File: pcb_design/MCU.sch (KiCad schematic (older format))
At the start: 14 parts, among them U1 STM32F40X_LQFP64, X2 ABM3B - 8MHz

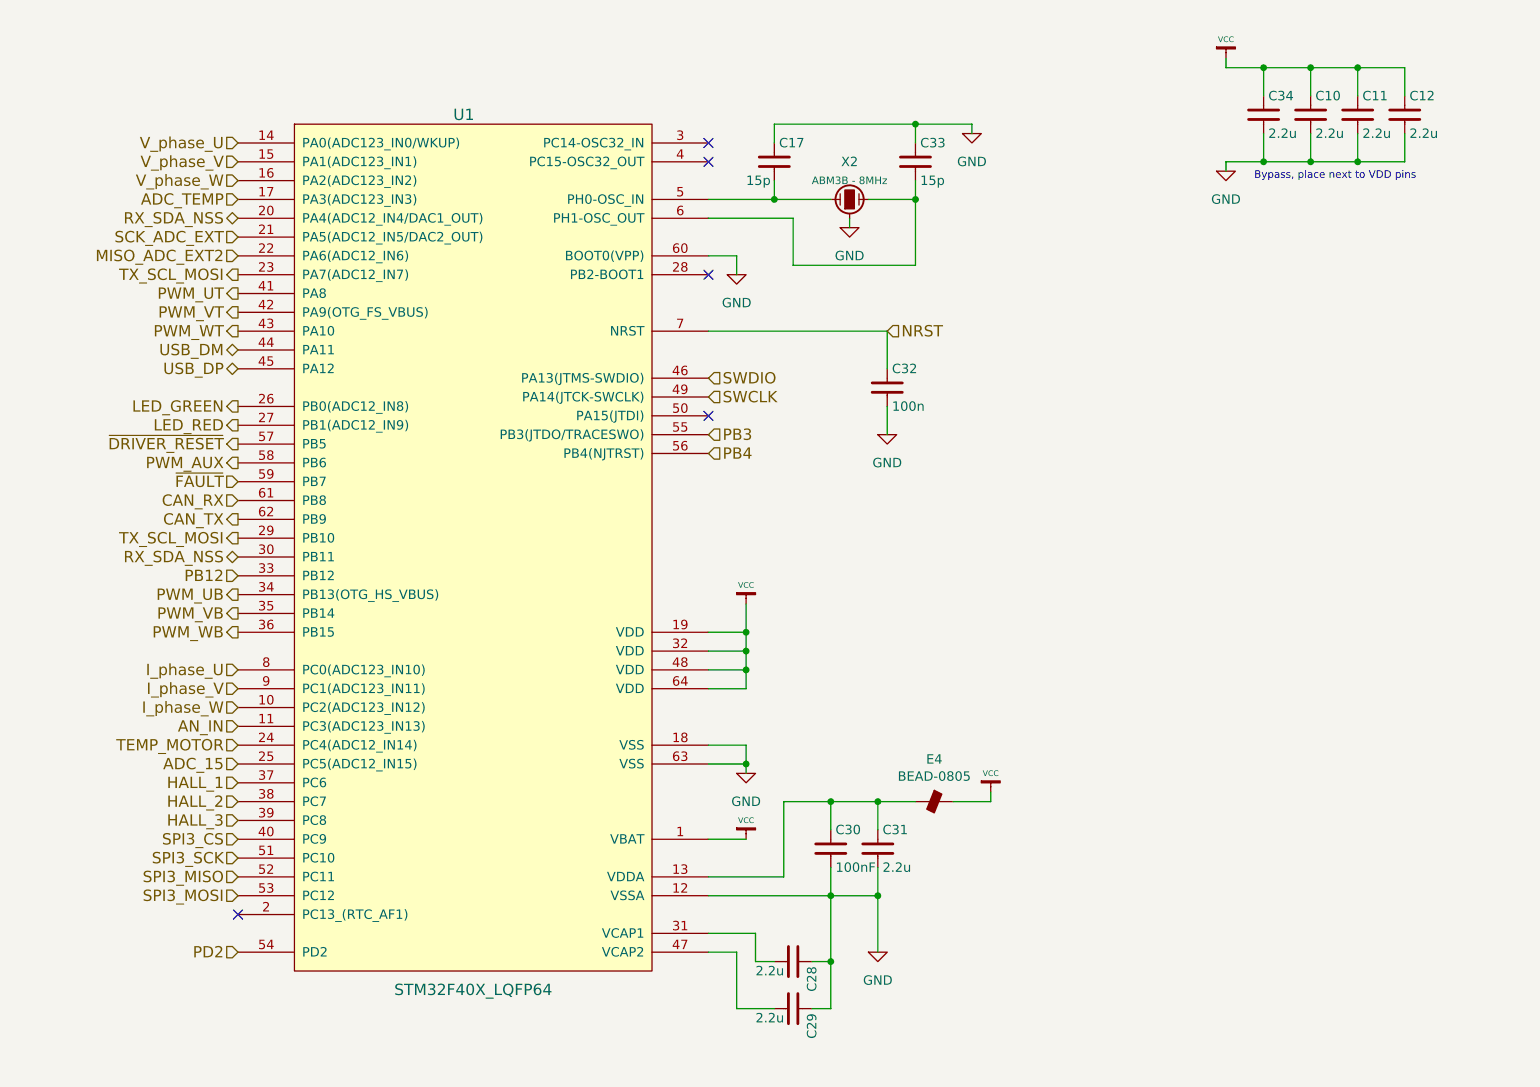
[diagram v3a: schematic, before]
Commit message: Added lp filters, fuses, tvs and power symbols
Signed-off-by: Marcos Chaparro <mchaparro@paltatech.com>
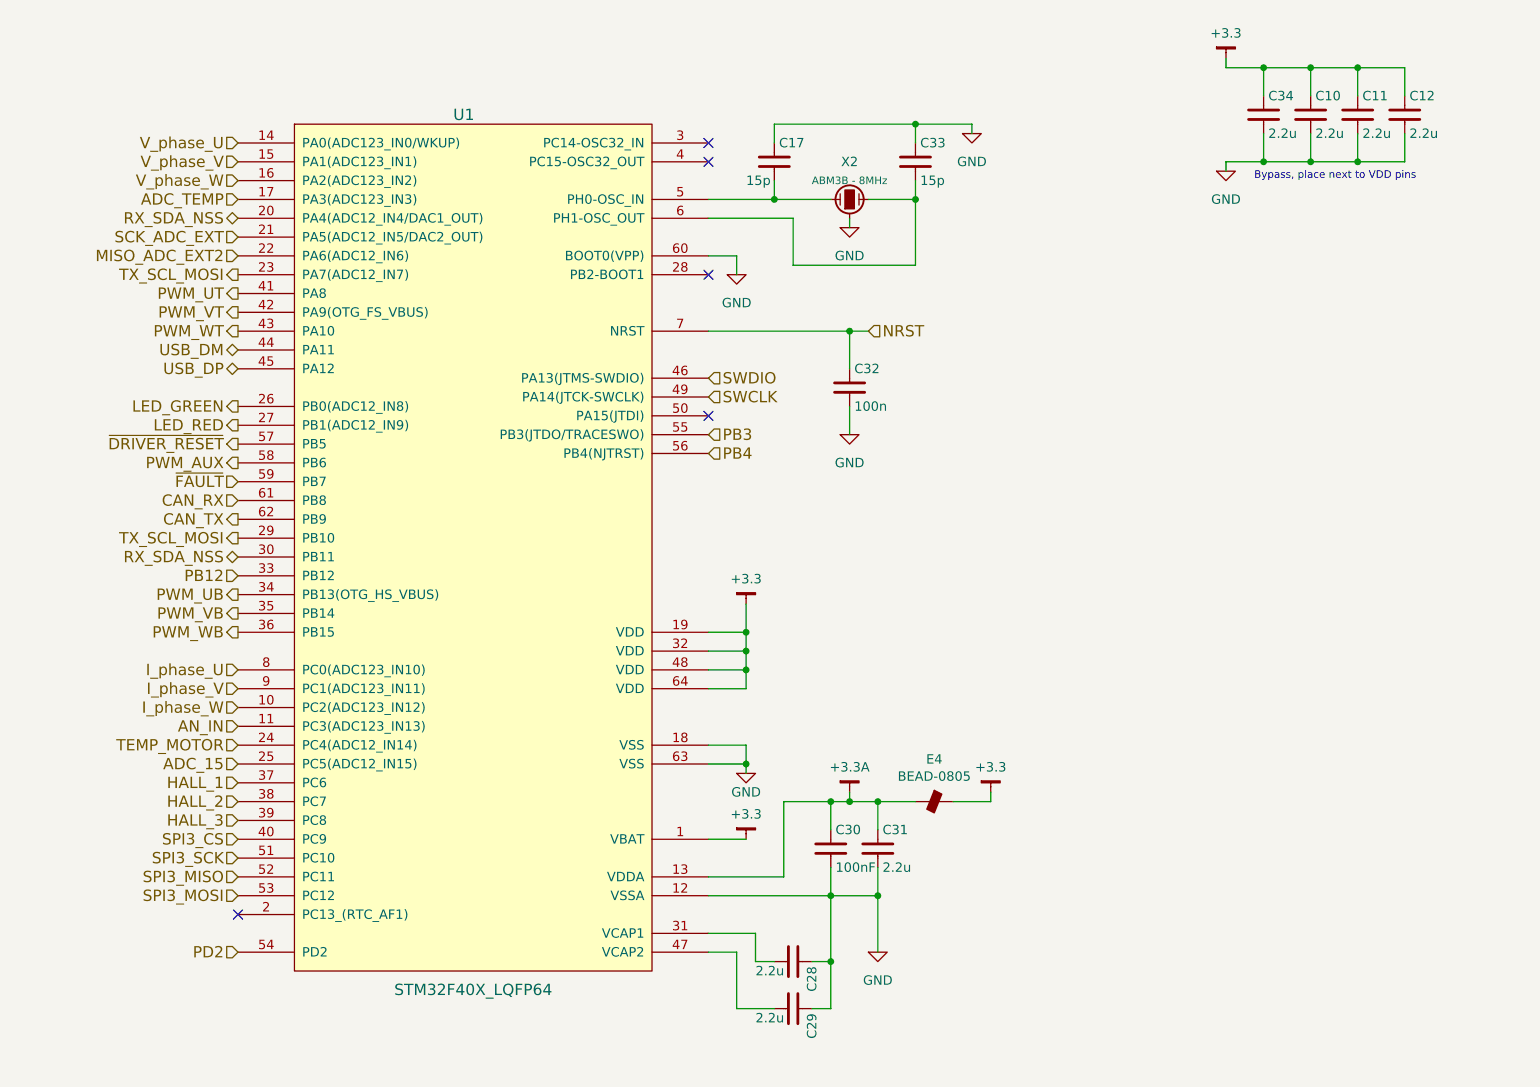
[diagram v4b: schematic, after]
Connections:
- net +3.3A: now reaches C30.1, C31.1, E4.1, U1.13 (VDDA)
- net VCC renamed +3.3
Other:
- moved on the sheet: C32
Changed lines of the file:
@@
 Text HLabel 3650 1900 0    60   3State ~ 0
 RX_SDA_NSS
-$Comp
-L VCC #PWR131
-U 1 1 572D84D8
-P 7650 4950
-F 0 "#PWR131" H 7650 5050 30  0001 C CNN
-F 1 "VCC" H 7650 5050 30  0000 C CNN
-F 2 "" H 7650 4950 60  0001 C CNN
-F 3 "" H 7650 4950 60  0001 C CNN
-	1    7650 4950
-	1    0    0    -1
-$EndComp
-$Comp
-L VCC #PWR124
-U 1 1 572D84D9
-P 6350 3950
-F 0 "#PWR124" H 6350 4050 30  0001 C CNN
-F 1 "VCC" H 6350 4050 30  0000 C CNN
-F 2 "" H 6350 3950 60  0001 C CNN
-F 3 "" H 6350 3950 60  0001 C CNN
-	1    6350 3950
-	1    0    0    -1
-$EndComp
 NoConn ~ 6150 2200
-$Comp
-L VCC #PWR126
-U 1 1 572D84DA
-P 6350 5200
-F 0 "#PWR126" H 6350 5300 30  0001 C CNN
-F 1 "VCC" H 6350 5300 30  0000 C CNN
-F 2 "" H 6350 5200 60  0001 C CNN
-F 3 "" H 6350 5200 60  0001 C CNN
-	1    6350 5200
-	1    0    0    -1
-$EndComp
 NoConn ~ 6150 2950
 NoConn ~ 6150 1500
@@
 Wire Wire Line
 	6800 6100 6700 6100
-$Comp
-L VCC #PWR132
-U 1 1 572D84DB
-P 8900 1050
-F 0 "#PWR132" H 8900 1150 30  0001 C CNN
-F 1 "VCC" H 8900 1150 30  0000 C CNN
-F 2 "" H 8900 1050 60  0001 C CNN
-F 3 "" H 8900 1050 60  0001 C CNN
-	1    8900 1050
-	1    0    0    -1
-$EndComp
 Connection ~ 9600 1600
 Wire Wire Line
@@
 	8900 1650 8900 1600
 Wire Wire Line
-	6150 2500 7100 2500
-Wire Wire Line
-	7100 2500 7100 2700
+	6150 2500 7000 2500
+Wire Wire Line
+	6900 2500 6900 2700
 Wire Wire Line
 	7250 2150 6600 2150
@@
 L C C32
 U 1 1 572D84E1
-P 7100 2800
-F 0 "C32" H 7125 2900 50  0000 L CNN
-F 1 "100n" H 7125 2700 50  0000 L CNN
-F 2 "IPC7351-Nominal:CAPC1608X55" H 7138 2650 30  0001 C CNN
-F 3 "" H 7100 2800 60  0000 C CNN
-	1    7100 2800
+P 6900 2800
+F 0 "C32" H 6925 2900 50  0000 L CNN
+F 1 "100n" H 6925 2700 50  0000 L CNN
+F 2 "IPC7351-Nominal:CAPC1608X55" H 6938 2650 30  0001 C CNN
+F 3 "" H 6900 2800 60  0000 C CNN
+	1    6900 2800
 	1    0    0    -1
 $EndComp
@@
 L GND #PWR129
 U 1 1 572D84E2
-P 7100 3050
-F 0 "#PWR129" H 7100 2800 50  0001 C CNN
-F 1 "GND" H 7100 2900 50  0000 C CNN
-F 2 "" H 7100 3050 60  0000 C CNN
-F 3 "" H 7100 3050 60  0000 C CNN
-	1    7100 3050
-	1    0    0    -1
-$EndComp
-Wire Wire Line
-	7100 3050 7100 2900
-Text HLabel 7100 2500 2    60   Input ~ 0
+P 6900 3050
+F 0 "#PWR129" H 6900 2800 50  0001 C CNN
+F 1 "GND" H 6900 2900 50  0000 C CNN
+F 2 "" H 6900 3050 60  0000 C CNN
+F 3 "" H 6900 3050 60  0000 C CNN
+	1    6900 3050
+	1    0    0    -1
+$EndComp
+Wire Wire Line
+	6900 3050 6900 2900
+Text HLabel 7000 2500 2    60   Input ~ 0
 NRST
 Text HLabel 6150 2750 2    60   Input ~ 0
@@
 P 6350 4850
 F 0 "#PWR125" H 6350 4600 50  0001 C CNN
-F 1 "GND" H 6350 4700 50  0000 C CNN
+F 1 "GND" H 6350 4750 50  0000 C CNN
 F 2 "" H 6350 4850 60  0000 C CNN
 F 3 "" H 6350 4850 60  0000 C CNN
@@
 	1    0    0    -1
 $EndComp
+$Comp
+L +3.3 #PWR?
+U 1 1 588B6A3F
+P 8900 1050
+F 0 "#PWR?" H 0   100 30  0001 C CNN
+F 1 "+3.3" H 8900 1183 50  0000 C CNN
+F 2 "" H 0   50  60  0000 C CNN
+F 3 "" H 0   50  60  0000 C CNN
+	1    8900 1050
+	1    0    0    -1
+$EndComp
+Connection ~ 6900 2500
+$Comp
+L +3.3 #PWR?
+U 1 1 588B6C25
+P 6350 3950
+F 0 "#PWR?" H 6400 4000 30  0001 C CNN
+F 1 "+3.3" H 6350 4083 50  0000 C CNN
+F 2 "" H 0   50  60  0000 C CNN
+F 3 "" H 0   50  60  0000 C CNN
+	1    6350 3950
+	1    0    0    -1
+$EndComp
+$Comp
+L +3.3 #PWR?
+U 1 1 588B6CC6
+P 7650 4950
+F 0 "#PWR?" H 7700 5000 30  0001 C CNN
+F 1 "+3.3" H 7650 5083 50  0000 C CNN
+F 2 "" H 0   50  60  0000 C CNN
+F 3 "" H 0   50  60  0000 C CNN
+	1    7650 4950
+	1    0    0    -1
+$EndComp
+$Comp
+L +3.3 #PWR?
+U 1 1 588B6D3A
+P 6350 5200
+F 0 "#PWR?" H 6400 5250 30  0001 C CNN
+F 1 "+3.3" H 6350 5333 50  0000 C CNN
+F 2 "" H -1300 300 60  0000 C CNN
+F 3 "" H -1300 300 60  0000 C CNN
+	1    6350 5200
+	1    0    0    -1
+$EndComp
+$Comp
+L +3.3A #PWR?
+U 1 1 588B9943
+P 6900 4950
+F 0 "#PWR?" H 6950 5000 30  0001 C CNN
+F 1 "+3.3A" H 6900 5083 50  0000 C CNN
+F 2 "" H -900 -500 60  0000 C CNN
+F 3 "" H -900 -500 60  0000 C CNN
+	1    6900 4950
+	1    0    0    -1
+$EndComp
+Wire Wire Line
+	6900 4950 6900 5000
+Connection ~ 6900 5000
 $EndSCHEMATC

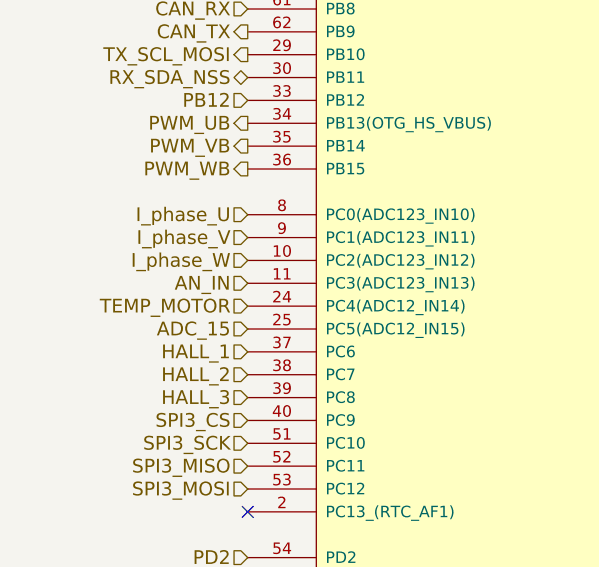
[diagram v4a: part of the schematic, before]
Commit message: Added bus voltage conditioning, %v to accel and regen inputs, regulator diode, annotated schematic
Signed-off-by: Marcos Chaparro <mchaparro@paltatech.com>
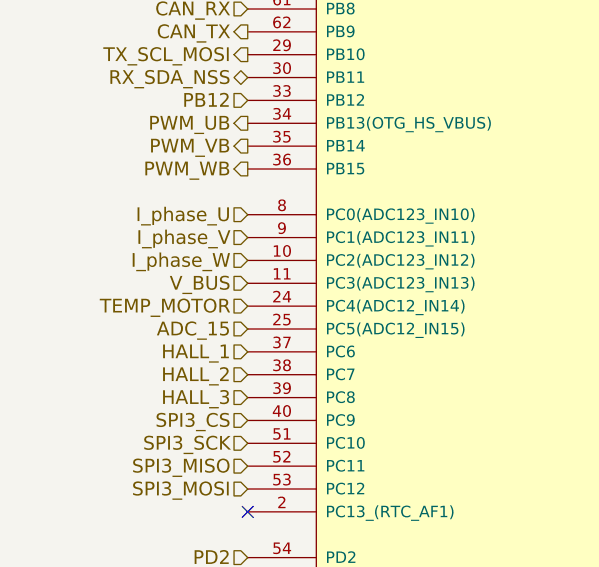
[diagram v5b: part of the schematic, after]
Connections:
- net AN_IN renamed V_BUS
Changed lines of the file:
@@
 $Descr A4 11693 8268
 encoding utf-8
-Sheet 12 12
+Sheet 12 13
 Title "VESC 6.4"
 Date "2016-07-07"
@@
 I_phase_U
 Text HLabel 3650 4600 0    60   Input ~ 0
-AN_IN
+V_BUS
 Text HLabel 3650 3100 0    60   Output ~ 0
 ~DRIVER_RESET
@@
 Bypass, place next to VDD pins
 $Comp
-L GND #PWR130
+L GND #PWR150
 U 1 1 572D84DC
 P 7550 1450
-F 0 "#PWR130" H 7550 1200 50  0001 C CNN
+F 0 "#PWR150" H 7550 1200 50  0001 C CNN
 F 1 "GND" H 7550 1300 50  0000 C CNN
 F 2 "" H 7550 1450 60  0000 C CNN
@@
 $EndComp
 $Comp
-L GND #PWR127
+L GND #PWR146
 U 1 1 572D84DF
 P 6900 1950
-F 0 "#PWR127" H 6900 1700 50  0001 C CNN
+F 0 "#PWR146" H 6900 1700 50  0001 C CNN
 F 1 "GND" H 6900 1800 50  0000 C CNN
 F 2 "" H 6900 1950 60  0000 C CNN
@@
 $EndComp
 $Comp
-L GND #PWR123
+L GND #PWR142
 U 1 1 572D84E0
 P 6300 2200
-F 0 "#PWR123" H 6300 1950 50  0001 C CNN
+F 0 "#PWR142" H 6300 1950 50  0001 C CNN
 F 1 "GND" H 6300 2050 50  0000 C CNN
 F 2 "" H 6300 2200 60  0000 C CNN
@@
 $EndComp
 $Comp
-L GND #PWR129
+L GND #PWR147
 U 1 1 572D84E2
 P 6900 3050
-F 0 "#PWR129" H 6900 2800 50  0001 C CNN
+F 0 "#PWR147" H 6900 2800 50  0001 C CNN
 F 1 "GND" H 6900 2900 50  0000 C CNN
 F 2 "" H 6900 3050 60  0000 C CNN
@@
 SWCLK
 $Comp
-L GND #PWR128
+L GND #PWR149
 U 1 1 572D84E3
 P 7050 5800
-F 0 "#PWR128" H 7050 5550 50  0001 C CNN
+F 0 "#PWR149" H 7050 5550 50  0001 C CNN
 F 1 "GND" H 7050 5650 50  0000 C CNN
 F 2 "" H 7050 5800 60  0000 C CNN
@@
 $EndComp
 $Comp
-L GND #PWR125
+L GND #PWR144
 U 1 1 572D84E4
 P 6350 4850
-F 0 "#PWR125" H 6350 4600 50  0001 C CNN
+F 0 "#PWR144" H 6350 4600 50  0001 C CNN
 F 1 "GND" H 6350 4750 50  0000 C CNN
 F 2 "" H 6350 4850 60  0000 C CNN
@@
 $EndComp
 $Comp
-L GND #PWR133
+L GND #PWR153
 U 1 1 572D84E9
 P 8900 1650
-F 0 "#PWR133" H 8900 1400 50  0001 C CNN
+F 0 "#PWR153" H 8900 1400 50  0001 C CNN
 F 1 "GND" H 8900 1500 50  0000 C CNN
 F 2 "" H 8900 1650 60  0000 C CNN
@@
 $EndComp
 $Comp
-L +3.3 #PWR?
+L +3.3 #PWR152
 U 1 1 588B6A3F
 P 8900 1050
-F 0 "#PWR?" H 0   100 30  0001 C CNN
+F 0 "#PWR152" H 0   100 30  0001 C CNN
 F 1 "+3.3" H 8900 1183 50  0000 C CNN
 F 2 "" H 0   50  60  0000 C CNN
@@
 Connection ~ 6900 2500
 $Comp
-L +3.3 #PWR?
+L +3.3 #PWR143
 U 1 1 588B6C25
 P 6350 3950
-F 0 "#PWR?" H 6400 4000 30  0001 C CNN
+F 0 "#PWR143" H 6400 4000 30  0001 C CNN
 F 1 "+3.3" H 6350 4083 50  0000 C CNN
 F 2 "" H 0   50  60  0000 C CNN
@@
 $EndComp
 $Comp
-L +3.3 #PWR?
+L +3.3 #PWR151
 U 1 1 588B6CC6
 P 7650 4950
-F 0 "#PWR?" H 7700 5000 30  0001 C CNN
+F 0 "#PWR151" H 7700 5000 30  0001 C CNN
 F 1 "+3.3" H 7650 5083 50  0000 C CNN
 F 2 "" H 0   50  60  0000 C CNN
@@
 $EndComp
 $Comp
-L +3.3 #PWR?
+L +3.3 #PWR145
 U 1 1 588B6D3A
 P 6350 5200
-F 0 "#PWR?" H 6400 5250 30  0001 C CNN
+F 0 "#PWR145" H 6400 5250 30  0001 C CNN
 F 1 "+3.3" H 6350 5333 50  0000 C CNN
 F 2 "" H -1300 300 60  0000 C CNN
@@
 $EndComp
 $Comp
-L +3.3A #PWR?
+L +3.3A #PWR148
 U 1 1 588B9943
 P 6900 4950
-F 0 "#PWR?" H 6950 5000 30  0001 C CNN
+F 0 "#PWR148" H 6950 5000 30  0001 C CNN
 F 1 "+3.3A" H 6900 5083 50  0000 C CNN
 F 2 "" H -900 -500 60  0000 C CNN
